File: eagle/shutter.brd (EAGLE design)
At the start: 32.7 x 21.6 mm, 18 parts, among them T1 BC547

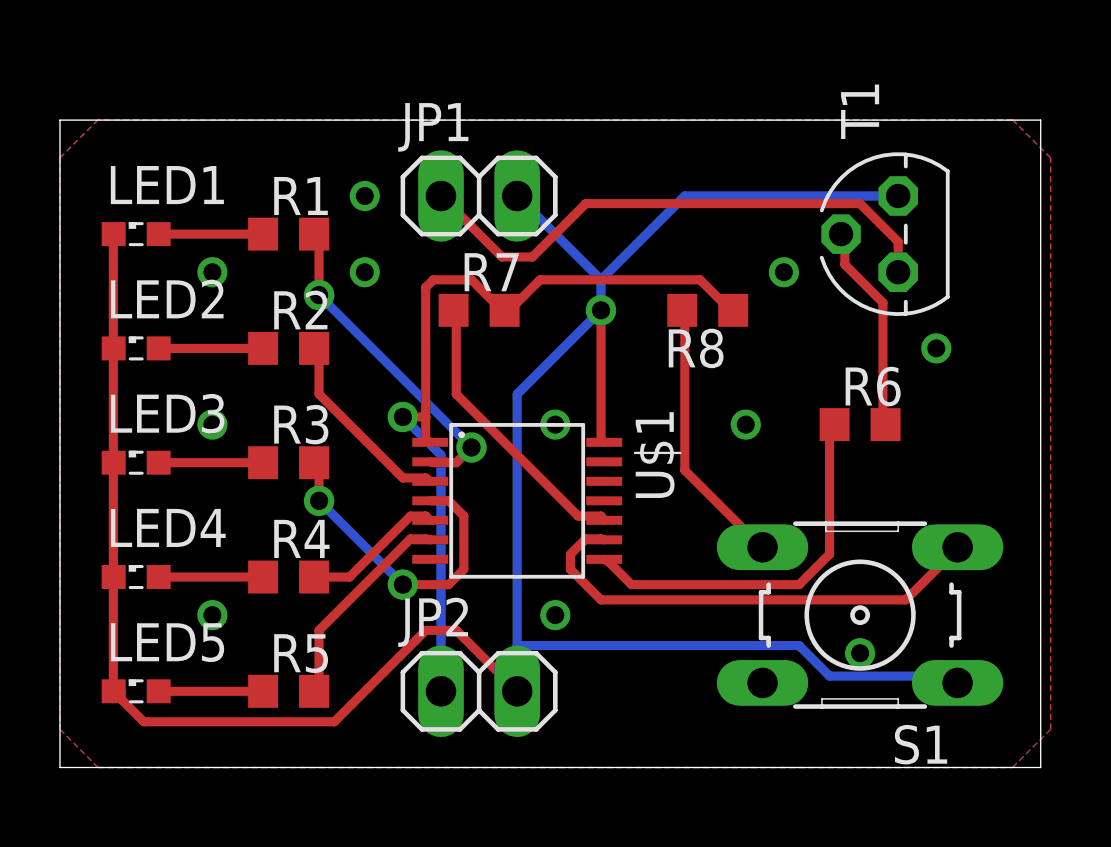
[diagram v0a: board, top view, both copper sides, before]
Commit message: fixed GND vias
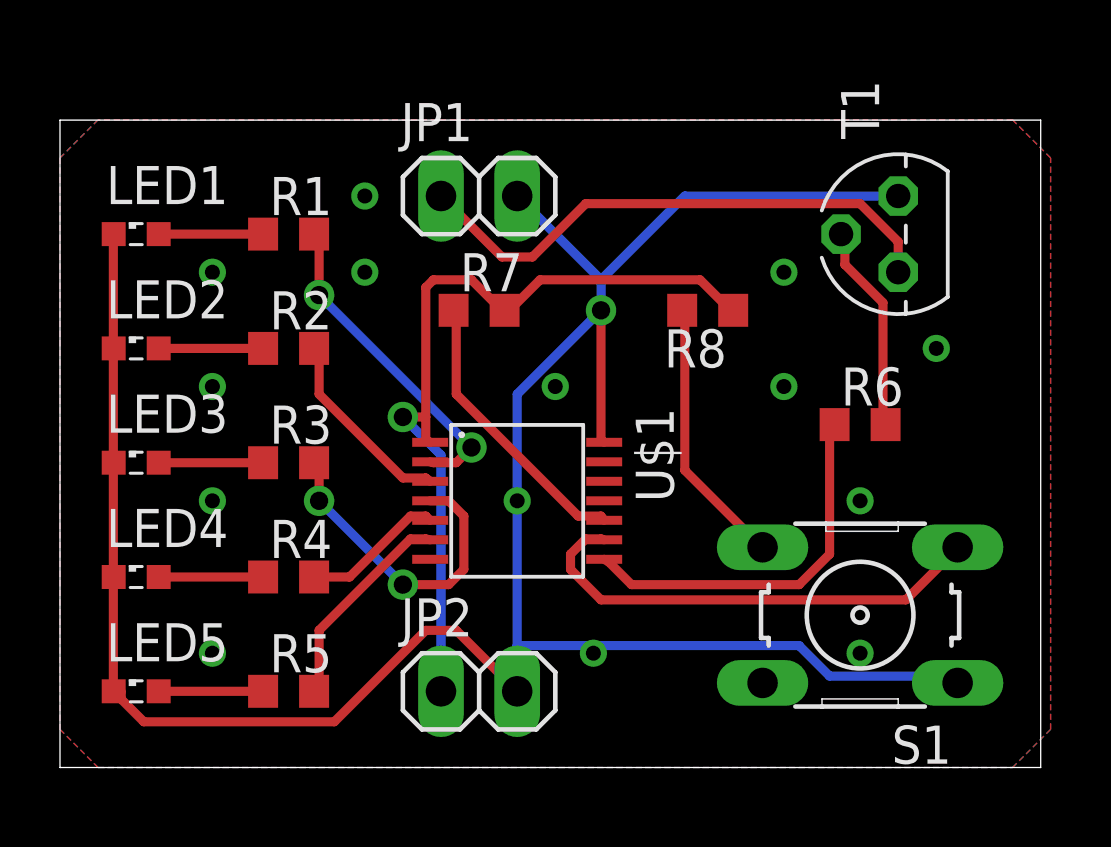
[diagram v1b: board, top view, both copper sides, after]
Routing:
- net GND: vias 1 -> 15
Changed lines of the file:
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@@
 <wire x1="20.828" y1="19.05" x2="27.94" y2="19.05" width="0.3048" layer="16"/>
 <wire x1="18.034" y1="16.256" x2="20.828" y2="19.05" width="0.3048" layer="16"/>
-<wire x1="15.24" y1="12.446" x2="15.24" y2="4.064" width="0.3048" layer="16"/>
+<wire x1="15.24" y1="12.446" x2="15.24" y2="8.89" width="0.3048" layer="16"/>
+<wire x1="15.24" y1="8.89" x2="15.24" y2="4.064" width="0.3048" layer="16"/>
 <wire x1="15.24" y1="4.064" x2="15.24" y2="2.54" width="0.3048" layer="16"/>
 <wire x1="18.034" y1="15.24" x2="15.24" y2="12.446" width="0.3048" layer="16"/>
@@
 <vertex x="31.75" y="21.59"/>
 </polygon>
+<via x="15.24" y="8.89" extent="1-16" drill="0.5" diameter="0.3048" shape="octagon"/>
+<via x="24.13" y="16.51" extent="1-16" drill="0.5" diameter="0.3048" shape="octagon"/>
+<via x="5.08" y="16.51" extent="1-16" drill="0.5" diameter="0.3048" shape="octagon"/>
+<via x="5.08" y="12.7" extent="1-16" drill="0.5" diameter="0.3048" shape="octagon"/>
+<via x="5.08" y="8.89" extent="1-16" drill="0.5" diameter="0.3048" shape="octagon"/>
+<via x="5.08" y="3.81" extent="1-16" drill="0.5" diameter="0.3048" shape="octagon"/>
+<via x="10.16" y="16.51" extent="1-16" drill="0.5" diameter="0.3048" shape="octagon"/>
+<via x="10.16" y="19.05" extent="1-16" drill="0.5" diameter="0.3048" shape="octagon"/>
+<via x="16.51" y="12.7" extent="1-16" drill="0.5" diameter="0.3048" shape="octagon"/>
+<via x="24.13" y="12.7" extent="1-16" drill="0.5" diameter="0.3048" shape="octagon"/>
+<via x="29.21" y="13.97" extent="1-16" drill="0.5" diameter="0.3048" shape="octagon"/>
+<via x="17.78" y="3.81" extent="1-16" drill="0.5" diameter="0.3048" shape="octagon"/>
+<via x="26.67" y="3.81" extent="1-16" drill="0.5" diameter="0.3048" shape="octagon"/>
+<via x="26.67" y="8.89" extent="1-16" drill="0.5" diameter="0.3048" shape="octagon"/>
+<wire x1="24.13" y1="12.7" x2="26.67" y2="8.89" width="0" layer="19" extent="1-1"/>
 </signal>
 <signal name="N$2">
@@
 <wire x1="12.7" y1="19.05" x2="14.732" y2="17.018" width="0.3048" layer="1"/>
 </signal>
-<signal name="N$1">
-<via x="16.51" y="11.43" extent="1-16" drill="0.6" shape="square"/>
-</signal>
-<signal name="N$18">
-<via x="22.86" y="11.43" extent="1-16" drill="0.6" shape="square"/>
-</signal>
-<signal name="N$19">
-<via x="5.08" y="11.43" extent="1-16" drill="0.6" shape="square"/>
-</signal>
-<signal name="N$21">
-<via x="5.08" y="16.51" extent="1-16" drill="0.6" shape="square"/>
-</signal>
-<signal name="N$22">
-<via x="10.16" y="16.51" extent="1-16" drill="0.6" shape="square"/>
-</signal>
-<signal name="N$23">
-<via x="24.13" y="16.51" extent="1-16" drill="0.6" shape="square"/>
-</signal>
-<signal name="N$24">
-<via x="16.51" y="5.08" extent="1-16" drill="0.6" shape="square"/>
-</signal>
-<signal name="N$25">
-<via x="5.08" y="5.08" extent="1-16" drill="0.6" shape="square"/>
-</signal>
-<signal name="N$26">
-<via x="10.16" y="19.05" extent="1-16" drill="0.6" shape="square"/>
-</signal>
-<signal name="N$27">
-<via x="29.21" y="13.97" extent="1-16" drill="0.6" shape="square"/>
-</signal>
-<signal name="N$28">
-<via x="26.67" y="3.81" extent="1-16" drill="0.6" shape="square"/>
-</signal>
 </signals>
